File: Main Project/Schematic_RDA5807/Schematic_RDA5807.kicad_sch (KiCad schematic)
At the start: 20 parts, among them SW1 SW_SPST, SW10 RotaryEncoder_Switch, SW11 Button, SW2 Button, SW3 Button, SW4 Button, SW5 Button, SW6 Button, SW7 Button, SW8 Button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

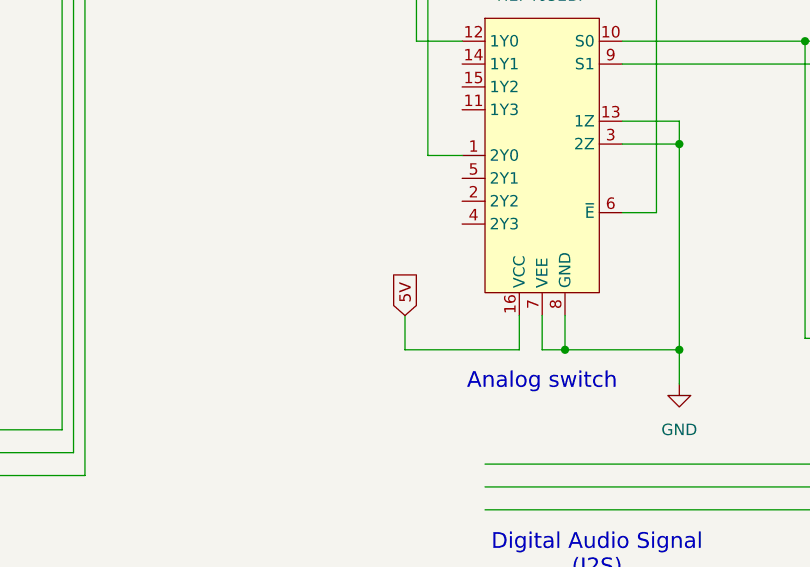
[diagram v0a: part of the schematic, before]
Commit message: Updates schematic
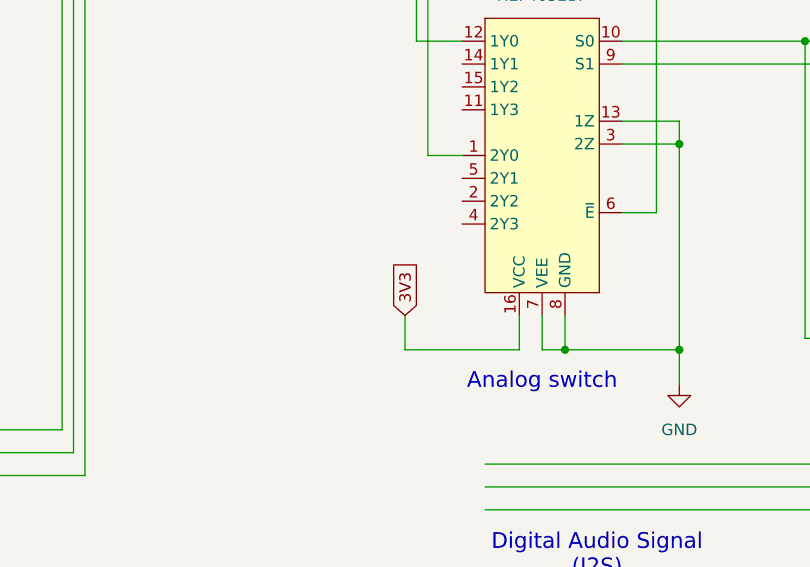
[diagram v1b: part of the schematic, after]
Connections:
- net 3V3: now also U7.16 (VCC)
- net 5V: no longer U7.16 (VCC)
- new net: U3. (ROUT-), U5. (XSMT), U7.10 (S0)
- new net: U3. (ROUT-), U5. (XSMT), U7.9 (S1)
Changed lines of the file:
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@@
 		)
 	)
-	(global_label "5V"
+	(global_label "3V3"
 		(shape input)
 		(at 133.35 160.02 90)

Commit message: updated schematic
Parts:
- added U6: ESP-WROOM-32, symbol DIP_symbols:ESP-WROOM-32
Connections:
- net GND: now also U7.10 (S0), U7.9 (S1), U6. (GND); no longer U7.13 (1Z), U7.3 (2Z)
- net at U1.8 (ADC1_7(SDA)), U2.1 (SDA), U4. (VCC): now also U6. (GND)
- net at U1.9 (ADC1_8(SCL)), U2.2 (SCK), U4. (VCC): now also U6. (GND)
- new net: U3. (ROUT-), U5. (XSMT), U7.13 (1Z)
- new net: U3. (ROUT-), U5. (XSMT), U7.3 (2Z)
- new net: U5. (XSMT), U6. (GND) (x3)
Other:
- note added: "Provide Bluetooth connection"

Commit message: Updated schematic (again)
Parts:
- removed U7: HEF4052BP, symbol DIP_symbols:74HC4052
- added U7: CD4066BE, symbol DIP_symbols:CD4066BE
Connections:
- net 5V: now also U7.14 (VDD)
- net GND: now also U7.7 (VSS)
- net at U2.7 (LOUT): now also U7.1 (A_I/O)
- net at U2.8 (ROUT): now also U7.3 (B_O/I)
- net at U1.14 (ADC2_3): now also U7.13 (CTRL_A), U7.5 (CTRL_B)
- new net: U3. (ROUT-), U5. (XSMT), U7.2 (A_O/I)
- new net: U3. (ROUT-), U5. (XSMT), U7.4 (B_I/O)
- new net: U5. (XSMT), U6. (GND) (x3)
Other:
- note added: "Provides Classic Bluetooth (Supports audio streaming)"
- note added: "Radio mode - ON Bluetooth mode - OFF"
- note removed: "Provide Bluetooth connection"
- note removed: "Radio mode - OFF Bluetooth mode - ON"

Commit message: Updated schematic
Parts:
- removed U6: ESP-WROOM-32, symbol DIP_symbols:ESP-WROOM-32
- added U8: ESP-WROOM-32, symbol DIP_symbols:ESP-WROOM-32
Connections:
- net 5V: now also U8. (GND)
- net GND: now also U8. (GND)
- net at U1.8 (ADC1_7(SDA)), U2.1 (SDA), U4. (VCC): now also U8. (GND)
- net at U1.9 (ADC1_8(SCL)), U2.2 (SCK), U4. (VCC): now also U8. (GND)
- new net: U3. (ROUT-), U5. (XSMT), U7.2 (A_O/I)
- new net: U3. (ROUT-), U5. (XSMT), U7.4 (B_I/O)
- new net: U5. (XSMT), U8. (GND) (x3)
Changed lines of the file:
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@@
 	(wire
 		(pts
+			(xy 231.14 49.53) (xy 231.14 44.45)
+		)
+		(stroke
+			(width 0)
+			(type default)
+		)
+	)
+	(wire
+		(pts
 			(xy 207.01 132.08) (xy 204.47 132.08)
 		)
@@
 	(wire
 		(pts
+			(xy 237.49 49.53) (xy 231.14 49.53)
+		)
+		(stroke
+			(width 0)
+			(type default)
+		)
+	)
+	(wire
+		(pts
 			(xy 30.48 57.15) (xy 30.48 120.65)
 		)
@@
 	(wire
 		(pts
-			(xy 231.14 69.85) (xy 231.14 74.93)
+			(xy 231.14 69.85) (xy 231.14 73.66)
 		)
 		(stroke
@@
 	(text "Provides Classic Bluetooth\n(Supports audio streaming)"
 		(exclude_from_sim no)
-		(at 254.762 45.72 0)
+		(at 259.08 40.132 0)
 		(effects
 			(font
@@
 	(global_label "5V"
 		(shape input)
+		(at 231.14 44.45 90)
+		(fields_autoplaced yes)
+		(effects
+			(font
+				(size 1.27 1.27)
+			)
+			(justify left)
+		)
+		(property "Intersheetrefs" "${INTERSHEET_REFS}"
+			(at 231.14 37.9572 90)
+			(effects
+				(font
+					(size 1.27 1.27)
+				)
+				(justify left)
+				(hide yes)
+			)
+		)
+	)
+	(global_label "5V"
+		(shape input)
 		(at 201.93 102.87 90)
 		(fields_autoplaced yes)
@@
 	(symbol
 		(lib_id "power:GND")
-		(at 231.14 74.93 0)
+		(at 231.14 73.66 0)
 		(unit 1)
 		(exclude_from_sim no)
@@
 		(fields_autoplaced yes)
 		(property "Reference" "#PWR011"
-			(at 231.14 81.28 0)
+			(at 231.14 80.01 0)
 			(effects
 				(font
@@
 		)
 		(property "Value" "GND"
-			(at 231.14 80.01 0)
+			(at 231.14 78.74 0)
 			(effects
 				(font
@@
 		)
 		(property "Footprint" ""
-			(at 231.14 74.93 0)
+			(at 231.14 73.66 0)
 			(effects
 				(font
@@
 		)
 		(property "Datasheet" ""
-			(at 231.14 74.93 0)
+			(at 231.14 73.66 0)
 			(effects
 				(font
@@
 		)
 		(property "Description" "Power symbol creates a global label with name \"GND\" , ground"
-			(at 231.14 74.93 0)
+			(at 231.14 73.66 0)
 			(effects
 				(font
@@
 	)
 	(symbol
-		(lib_id "DIP_symbols:ESP-WROOM-32")
-		(at 247.65 46.99 0)
-		(unit 1)
-		(exclude_from_sim no)
-		(in_bom yes)
-		(on_board yes)
-		(dnp no)
-		(fields_autoplaced yes)
-		(property "Reference" "U6"
-			(at 256.54 60.1979 0)
-			(effects
-				(font
-					(size 1.27 1.27)
-				)
-				(justify left)
-			)
-		)
-		(property "Value" "ESP-WROOM-32"
-			(at 256.54 62.7379 0)
-			(effects
-				(font
-					(size 1.27 1.27)
-				)
-				(justify left)
-			)
-		)
-		(property "Footprint" ""
-			(at 247.65 46.99 0)
-			(effects
-				(font
-					(size 1.27 1.27)
-				)
-				(hide yes)
-			)
-		)
-		(property "Datasheet" ""
-			(at 247.65 46.99 0)
-			(effects
-				(font
-					(size 1.27 1.27)
-				)
-				(hide yes)
-			)
-		)
-		(property "Description" ""
-			(at 247.65 46.99 0)
-			(effects
-				(font
-					(size 1.27 1.27)
-				)
-				(hide yes)
-			)
-		)
-		(pin ""
-		)
-		(pin ""
-		)
-		(pin ""
-		)
-		(pin ""
-		)
-		(pin ""
-		)
-		(pin ""
-		)
-		(instances
-			(project ""
-				(path "/e4ac0108-b4d8-4685-aa5b-dfce1ac93b82"
-					(reference "U6")
-					(unit 1)
-				)
-			)
-		)
-	)
-	(symbol
 		(lib_id "Switch:SW_Push")
 		(at 25.4 135.89 90)
@@
 					(unit 1)
 				)
+			)
+		)
+	)
+	(symbol
+		(lib_name "ESP-WROOM-32_1")
+		(lib_id "DIP_symbols:ESP-WROOM-32")
+		(at 247.65 44.45 0)
+		(unit 1)
+		(exclude_from_sim no)
+		(in_bom yes)
+		(on_board yes)
+		(dnp no)
+		(fields_autoplaced yes)
+		(property "Reference" "U8"
+			(at 256.54 58.4199 0)
+			(effects
+				(font
+					(size 1.27 1.27)
+				)
+				(justify left)
+			)
+		)
+		(property "Value" "ESP-WROOM-32"
+			(at 256.54 60.9599 0)
+			(effects
+				(font
+					(size 1.27 1.27)
+				)
+				(justify left)
+			)
+		)
+		(property "Footprint" ""
+			(at 247.65 44.45 0)
+			(effects
+				(font
+					(size 1.27 1.27)
+				)
+				(hide yes)
+			)
+		)
+		(property "Datasheet" ""
+			(at 247.65 44.45 0)
+			(effects
+				(font
+					(size 1.27 1.27)
+				)
+				(hide yes)
+			)
+		)
+		(property "Description" ""
+			(at 247.65 44.45 0)
+			(effects
+				(font
+					(size 1.27 1.27)
+				)
+				(hide yes)
+			)
+		)
+		(pin ""
+		)
+		(pin ""
+		)
+		(pin ""
+		)
+		(pin ""
+		)
+		(pin ""
+		)
+		(pin ""
+		)
+		(pin ""
+		)
+		(instances
+			(project ""
+				(path "/e4ac0108-b4d8-4685-aa5b-dfce1ac93b82"
+					(reference "U8")
+					(unit 1)
+				)

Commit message: Updated schematic
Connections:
- net 3V3: no longer U5. (XSMT)
- net 5V: now also U5. (XSMT)
- new net: U3. (ROUT-), U5. (XSMT), U7.2 (A_O/I)
- new net: U3. (ROUT-), U5. (XSMT), U7.4 (B_I/O)
- new net: U5. (XSMT), U8. (GND) (x3)
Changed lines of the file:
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@@
 		)
 	)
-	(global_label "3V3"
+	(global_label "5V"
 		(shape input)
 		(at 198.12 171.45 90)

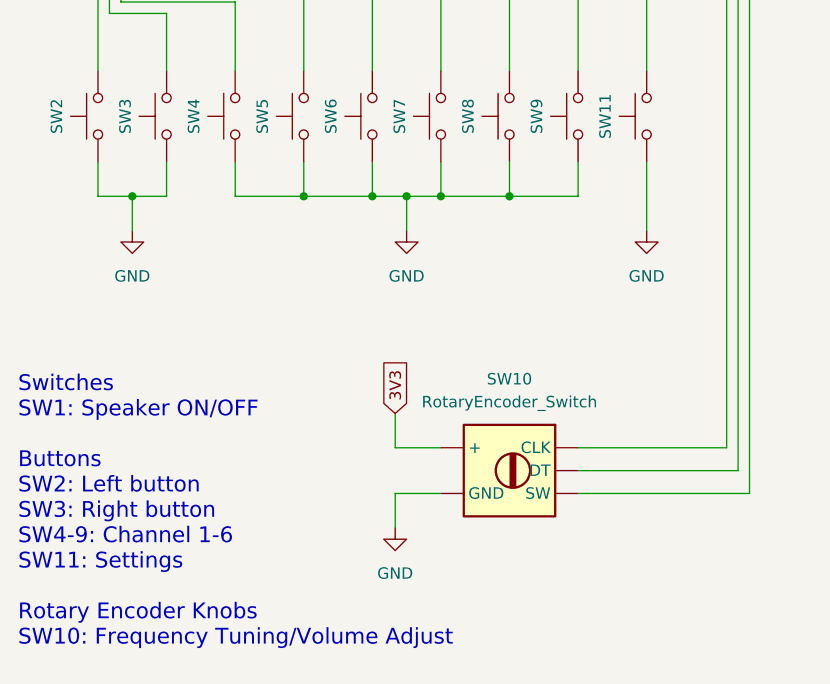
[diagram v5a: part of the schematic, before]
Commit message: Updated schematic, changes button functions
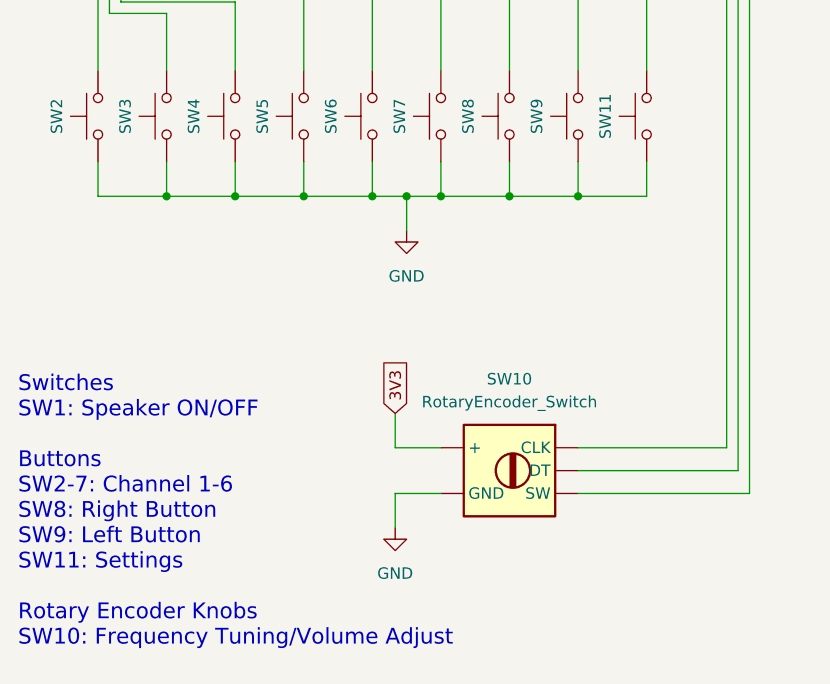
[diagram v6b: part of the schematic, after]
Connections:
- new net: U3. (ROUT-), U5. (XSMT), U7.2 (A_O/I)
- new net: U3. (ROUT-), U5. (XSMT), U7.4 (B_I/O)
- new net: U5. (XSMT), U8. (GND) (x3)
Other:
- note added: "Switches SW1: Speaker ON/OFF Buttons SW2-7: Channel 1-6 SW8: Right Button SW9: Left Button SW11: Settings Rotary Encoder Knobs SW10: Frequency Tuning/Volume Adjust"
- note removed: "Switches SW1: Speaker ON/OFF Buttons SW2: Left button SW3: Right button SW4-9: Channel 1-6 SW11: Settings Rotary Encoder Knobs SW10: Frequency Tuning/Volume Adjust"
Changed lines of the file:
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@@
 	)
 	(junction
+		(at 33.02 144.78)
+		(diameter 0)
+		(color 0 0 0 0)
+	)
+	(junction
 		(at 120.65 21.59)
 		(diameter 0)
@@
 	)
 	(junction
-		(at 29.21 144.78)
+		(at 78.74 144.78)
 		(diameter 0)
 		(color 0 0 0 0)
@@
 		(color 0 0 0 0)
 	)
+	(junction
+		(at 40.64 144.78)
+		(diameter 0)
+		(color 0 0 0 0)
+	)
 	(wire
 		(pts
@@
 	(wire
 		(pts
-			(xy 25.4 144.78) (xy 29.21 144.78)
+			(xy 25.4 144.78) (xy 33.02 144.78)
 		)
 		(stroke
@@
 	(wire
 		(pts
-			(xy 29.21 148.59) (xy 29.21 144.78)
-		)
-		(stroke
-			(width 0)
-			(type default)
-		)
-	)
-	(wire
-		(pts
 			(xy 179.07 134.62) (xy 207.01 134.62)
 		)
@@
 	(wire
 		(pts
-			(xy 86.36 140.97) (xy 86.36 148.59)
+			(xy 86.36 140.97) (xy 86.36 144.78)
 		)
 		(stroke
@@
 	(wire
 		(pts
+			(xy 78.74 144.78) (xy 86.36 144.78)
+		)
+		(stroke
+			(width 0)
+			(type default)
+		)
+	)
+	(wire
+		(pts
 			(xy 45.72 107.95) (xy 95.25 107.95)
 		)
@@
 	(wire
 		(pts
-			(xy 29.21 144.78) (xy 33.02 144.78)
+			(xy 58.42 172.72) (xy 58.42 168.91)
 		)
 		(stroke
@@
 	(wire
 		(pts
-			(xy 58.42 172.72) (xy 58.42 168.91)
+			(xy 154.94 57.15) (xy 154.94 64.77)
 		)
 		(stroke
@@
 	(wire
 		(pts
-			(xy 154.94 57.15) (xy 154.94 64.77)
+			(xy 33.02 144.78) (xy 40.64 144.78)
 		)
 		(stroke
@@
 		)
 	)
-	(text "Switches\nSW1: Speaker ON/OFF\n\nButtons\nSW2: Left button\nSW3: Right button\nSW4-9: Channel 1-6\nSW11: Settings\n\nRotary Encoder Knobs\nSW10: Frequency Tuning/Volume Adjust"
+	(text "Switches\nSW1: Speaker ON/OFF\n\nButtons\nSW2-7: Channel 1-6\nSW8: Right Button\nSW9: Left Button\nSW11: Settings\n\nRotary Encoder Knobs\nSW10: Frequency Tuning/Volume Adjust"
 		(exclude_from_sim no)
 		(at 16.51 179.832 0)
@@
 	(symbol
 		(lib_id "power:GND")
-		(at 29.21 148.59 0)
-		(unit 1)
-		(exclude_from_sim no)
-		(in_bom yes)
-		(on_board yes)
-		(dnp no)
-		(fields_autoplaced yes)
-		(property "Reference" "#PWR08"
-			(at 29.21 154.94 0)
-			(effects
-				(font
-					(size 1.27 1.27)
-				)
-				(hide yes)
-			)
-		)
-		(property "Value" "GND"
-			(at 29.21 153.67 0)
-			(effects
-				(font
-					(size 1.27 1.27)
-				)
-			)
-		)
-		(property "Footprint" ""
-			(at 29.21 148.59 0)
-			(effects
-				(font
-					(size 1.27 1.27)
-				)
-				(hide yes)
-			)
-		)
-		(property "Datasheet" ""
-			(at 29.21 148.59 0)
-			(effects
-				(font
-					(size 1.27 1.27)
-				)
-				(hide yes)
-			)
-		)
-		(property "Description" "Power symbol creates a global label with name \"GND\" , ground"
-			(at 29.21 148.59 0)
-			(effects
-				(font
-					(size 1.27 1.27)
-				)
-				(hide yes)
-			)
-		)
-		(pin "1"
-		)
-		(instances
-			(project "Schematic_RDA5807"
-				(path "/e4ac0108-b4d8-4685-aa5b-dfce1ac93b82"
-					(reference "#PWR08")
-					(unit 1)
-				)
-			)
-		)
-	)
-	(symbol
-		(lib_id "power:GND")
 		(at 59.69 148.59 0)
 		(unit 1)
@@
 					(unit 1)
 				)
-			)
-		)
-	)
-	(symbol
-		(lib_id "power:GND")
-		(at 86.36 148.59 0)
-		(unit 1)
-		(exclude_from_sim no)
-		(in_bom yes)
-		(on_board yes)
-		(dnp no)
-		(fields_autoplaced yes)
-		(property "Reference" "#PWR010"
-			(at 86.36 154.94 0)
-			(effects
-				(font
-					(size 1.27 1.27)
-				)
-				(hide yes)
-			)
-		)
-		(property "Value" "GND"
-			(at 86.36 153.67 0)
-			(effects
-				(font
-					(size 1.27 1.27)
-				)
-			)
-		)
-		(property "Footprint" ""
-			(at 86.36 148.59 0)
-			(effects
-				(font
-					(size 1.27 1.27)
-				)
-				(hide yes)
-			)
-		)
-		(property "Datasheet" ""
-			(at 86.36 148.59 0)
-			(effects
-				(font
-					(size 1.27 1.27)
-				)
-				(hide yes)
-			)
-		)
-		(property "Description" "Power symbol creates a global label with name \"GND\" , ground"
-			(at 86.36 148.59 0)
-			(effects
-				(font
-					(size 1.27 1.27)
-				)
-				(hide yes)
-			)
-		)
-		(pin "1"
-		)
-		(instances
-			(project "Schematic_RDA5807"
-				(path "/e4ac0108-b4d8-4685-aa5b-dfce1ac93b82"
-					(reference "#PWR010")
-					(unit 1)
-				)
